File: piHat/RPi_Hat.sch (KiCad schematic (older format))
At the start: 5 parts, among them J1 RPi_GPIO

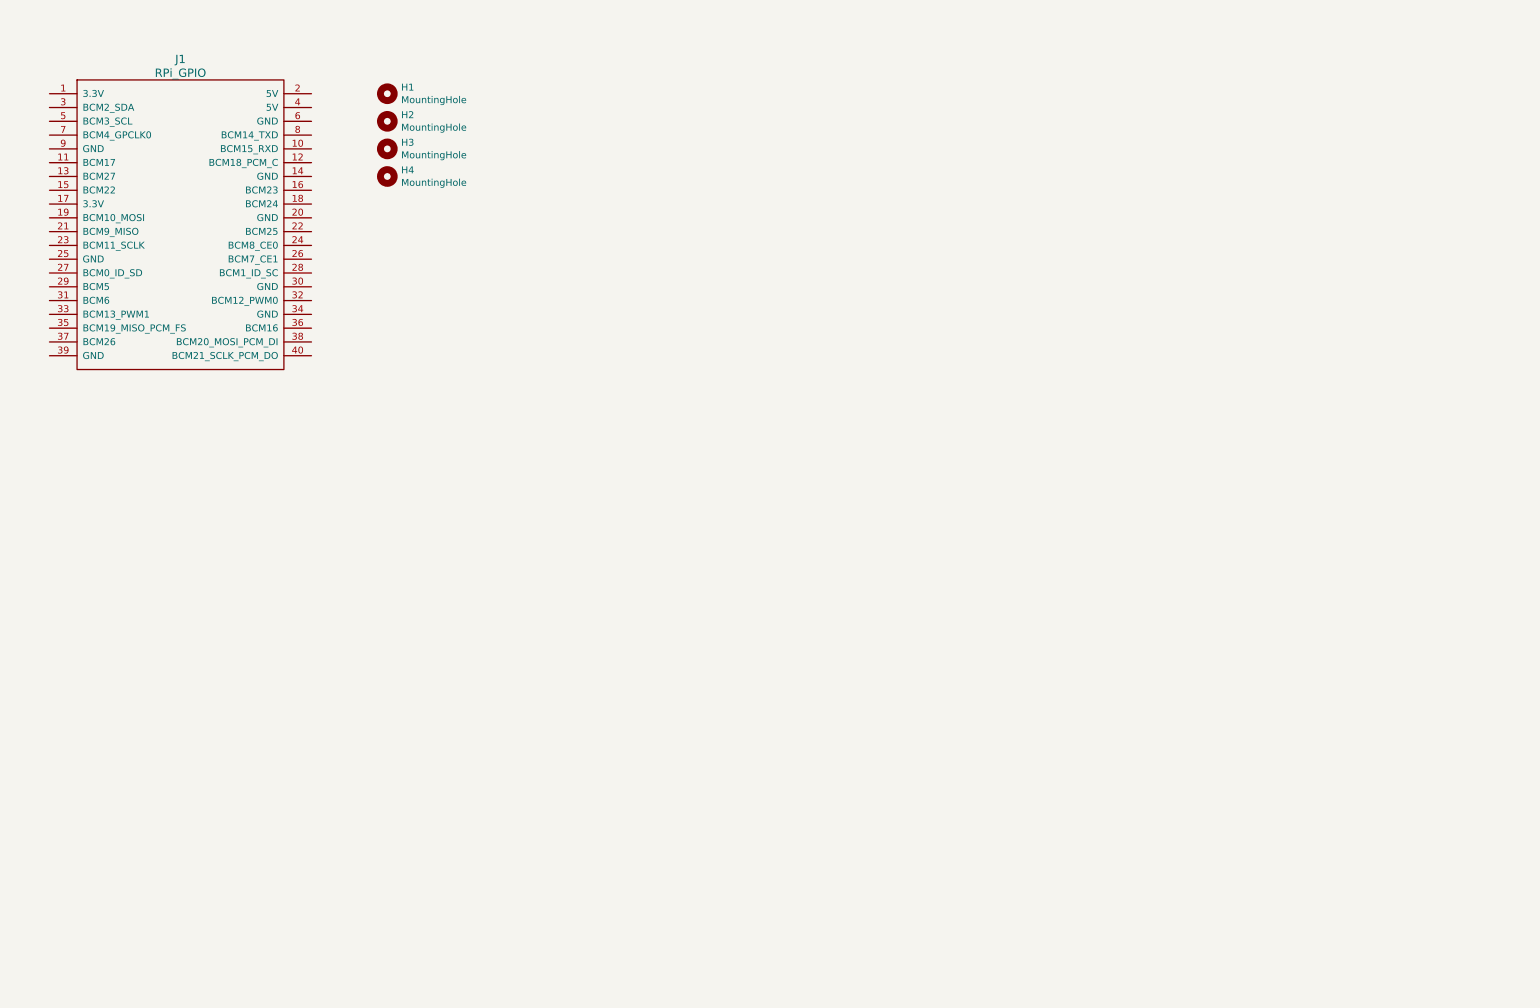
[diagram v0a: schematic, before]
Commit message: add pi HAT schematic (spid hat as template)
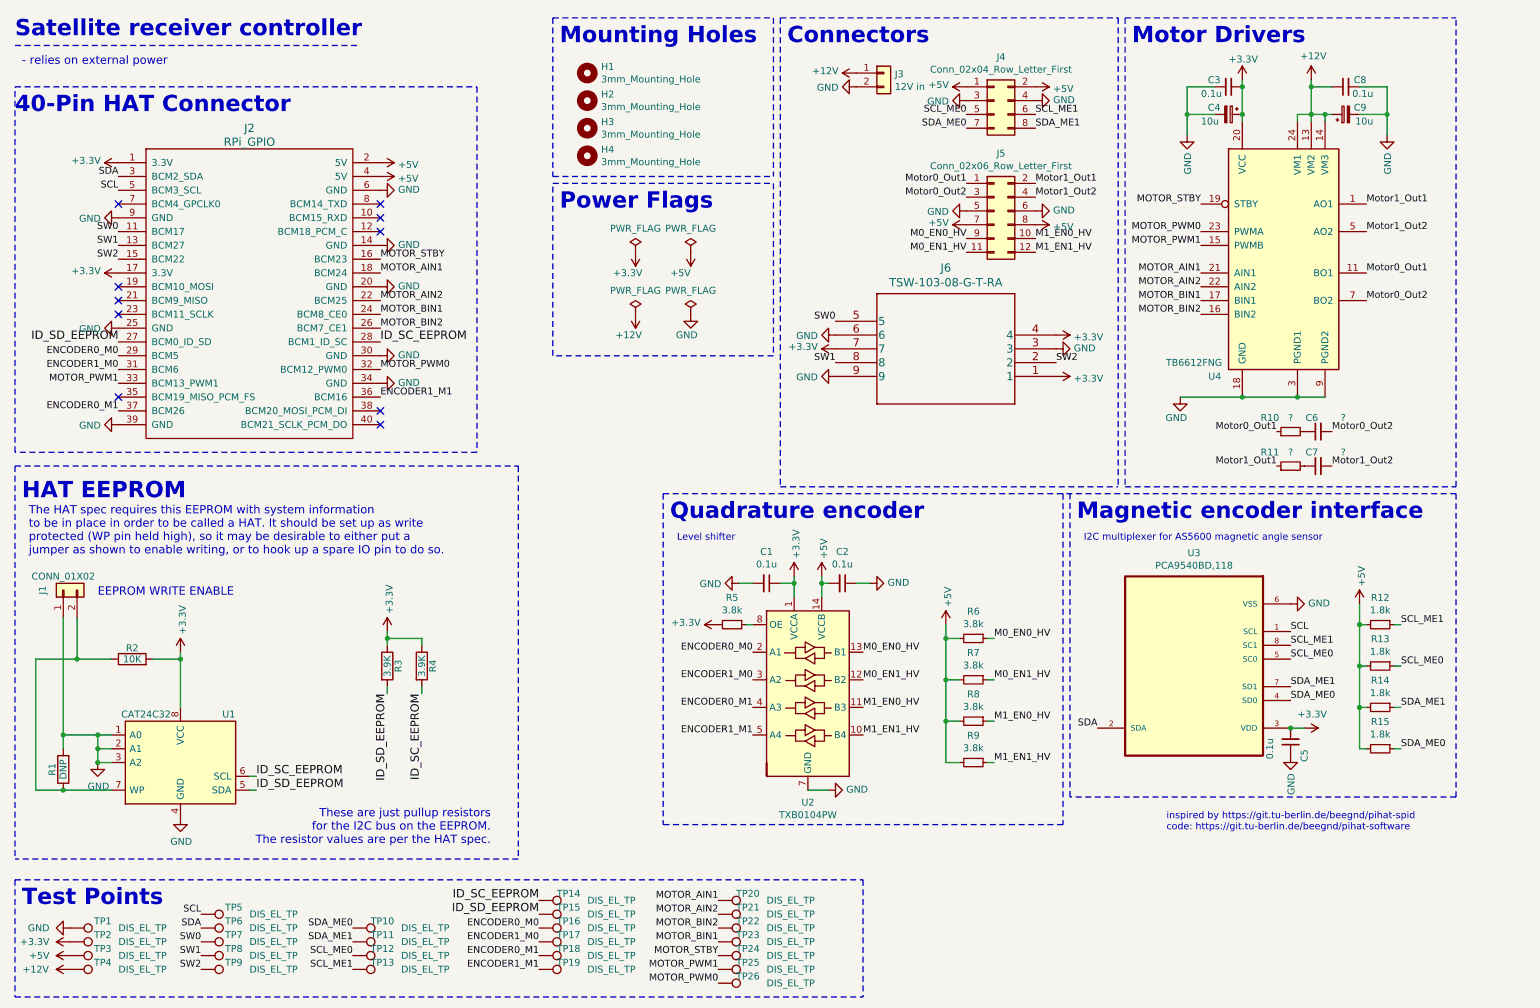
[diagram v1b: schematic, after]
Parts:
- added C1, C2, C3, C5, C8: 0.1u, Capacitor_SMD:C_0805_2012Metric_Pad1.18x1.45mm_HandSolder, symbol Device:C_Small
- added C4, C9: 10u, Capacitor_SMD:C_0805_2012Metric_Pad1.18x1.45mm_HandSolder, symbol Device:CP_Small
- added C6, C7: ?, Capacitor_SMD:C_0805_2012Metric_Pad1.18x1.45mm_HandSolder, symbol Device:C_Small
- added J1: CONN_01X02, Connector_PinHeader_2.54mm:PinHeader_1x02_P2.54mm_Vertical, symbol Connector_Generic:Conn_01x02
- added J3: 12V in, Connector_PinHeader_2.54mm:PinHeader_1x02_P2.54mm_Horizontal, symbol Connector_Generic:Conn_01x02
- added J4: Conn_02x04_Row_Letter_First, Connector_PinHeader_2.54mm:PinHeader_2x04_P2.54mm_Horizontal, symbol Connector_Generic:Conn_02x04_Odd_Even
- added J5: Conn_02x06_Row_Letter_First, Connector_PinHeader_2.54mm:PinHeader_2x06_P2.54mm_Horizontal, symbol Connector_Generic:Conn_02x06_Odd_Even
- added J6: TSW-103-08-G-T-RA, piHat:TSW-103-08-G-T-RA, symbol RPi_Hat:TSW-103-08-G-T-RA
- added R1: DNP, Resistor_SMD:R_0805_2012Metric_Pad1.20x1.40mm_HandSolder, symbol Device:R
- added R10, R11: ?, Resistor_SMD:R_0805_2012Metric_Pad1.20x1.40mm_HandSolder, symbol Device:R_Small
- added R12, R13, R14, R15: 1.8k, Resistor_SMD:R_0805_2012Metric_Pad1.20x1.40mm_HandSolder, symbol Device:R_Small
- added R2: 10K, Resistor_SMD:R_0805_2012Metric_Pad1.20x1.40mm_HandSolder, symbol Device:R
- added R3, R4: 3.9K, Resistor_SMD:R_0805_2012Metric_Pad1.20x1.40mm_HandSolder, symbol Device:R
- added R5, R6, R7, R8, R9: 3.8k, Resistor_SMD:R_0805_2012Metric_Pad1.20x1.40mm_HandSolder, symbol Device:R_Small
- added TP1, TP10, TP11, TP12, TP13, TP14, TP15, TP16, TP17, TP18, TP19, TP2, TP20, TP21, TP22, TP23, TP24, TP25, TP26, TP3, TP4, TP5, TP6, TP7, TP8, TP9: DIS_EL_TP, TestPoint:TestPoint_Pad_D1.0mm, symbol Connector:TestPoint
- added U1: CAT24C32, Package_SO:SOIC-8_3.9x4.9mm_P1.27mm, symbol RPi_Hat:CAT24C32-raspberrypi_hat
- added U2: TXB0104PW, Package_SO:TSSOP-14_4.4x5mm_P0.65mm, symbol Logic_LevelTranslator:TXB0104PW
- added U3: PCA9540BD,118, SOIC127P600X175-8N, symbol RPi_Hat:PCA9540BD,118
- added U4: TB6612FNG, Package_SO:SSOP-24_5.3x8.2mm_P0.65mm, symbol Driver_Motor:TB6612FNG
- H1, H2, H3, H4: value MountingHole -> 3mm_Mounting_Hole; Digikey Part Number (none) -> -; Manufacturer_Part_Number (none) -> -; Mouser Part Number (none) -> -
- J2: renamed from J1; Digikey Part Number (none) -> 1528-1785-ND; Manufacturer_Part_Number (none) -> 2222; Mouser Part Number (none) -> 485-2222
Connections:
- net +3V3: now reaches J2.1 (3.3V)
- net +3V3: now also J2.17 (3.3V), C1.1, C3.1, C4.1, C5.2, J6.1, J6.4, J6.7, R2.2, R3.1, R4.1, R5.2, TP2.1, U1.8 (VCC), U2.1 (VCCA), U3.3 (VDD), U4.20 (VCC)
- net SW0: now reaches J2.11 (BCM17)
- net SW0: now also J6.5, TP7.1
- net SW1: now reaches J2.13 (BCM27)
- net SW1: now also J6.8, TP8.1
- net GND: now reaches J2.14 (GND)
- net GND: now also J2.20 (GND), J2.25 (GND), J2.30 (GND), J2.34 (GND), J2.39 (GND), J2.6 (GND), J2.9 (GND), C1.2, C2.1, C3.2, C4.2, C5.1, C8.2, C9.2, J1.1 (Pin_1), J3.2 (Pin_2), J4.3 (Pin_3), J4.4 (Pin_4), J5.5 (Pin_5), J5.6 (Pin_6), J6.3, J6.6, J6.9, R1.2, TP1.1, U1.1 (A0), U1.2 (A1), U1.3 (A2), U1.4 (GND), U2.7 (GND), U3.6 (VSS), U4.10 (PGND2), U4.18 (GND), U4.3 (PGND1), U4.4 (PGND1), U4.9 (PGND2)
- net SW2: now reaches J2.15 (BCM22)
- net SW2: now also J6.2, TP9.1
- net MOTOR_STBY: now reaches J2.16 (BCM23)
- net MOTOR_STBY: now also TP24.1, U4.19 (STBY)
- net MOTOR_AIN1: now reaches J2.18 (BCM24)
- net MOTOR_AIN1: now also TP20.1, U4.21 (AIN1)
- net +5V: now reaches J2.2 (5V)
- net +5V: now also J2.4 (5V), C2.2, J4.1 (Pin_1), J4.2 (Pin_2), J5.7 (Pin_7), J5.8 (Pin_8), R12.2, R13.2, R14.2, R15.2, R6.2, R7.2, R8.2, R9.2, TP3.1, U2.14 (VCCB)
- net MOTOR_AIN2: now reaches J2.22 (BCM25)
- net MOTOR_AIN2: now also TP21.1, U4.22 (AIN2)
- net MOTOR_BIN1: now reaches J2.24 (BCM8_CE0)
- net MOTOR_BIN1: now also TP23.1, U4.17 (BIN1)
- net MOTOR_BIN2: now reaches J2.26 (BCM7_CE1)
- net MOTOR_BIN2: now also TP22.1, U4.16 (BIN2)
- net ID_SD_EEPROM: now reaches J2.27 (BCM0_ID_SD)
- net ID_SD_EEPROM: now also R3.2, TP15.1, U1.5 (SDA)
- net ID_SC_EEPROM: now reaches J2.28 (BCM1_ID_SC)
- net ID_SC_EEPROM: now also R4.2, TP14.1, U1.6 (SCL)
- net ENCODER0_M0: now reaches J2.29 (BCM5)
- net ENCODER0_M0: now also TP16.1, U2.2 (A1)
- net SDA: now reaches J2.3 (BCM2_SDA)
- net SDA: now also TP6.1, U3.2 (SDA)
- net ENCODER1_M0: now reaches J2.31 (BCM6)
- net ENCODER1_M0: now also TP17.1, U2.3 (A2)
- net MOTOR_PWM0: now reaches J2.32 (BCM12_PWM0)
- net MOTOR_PWM0: now also TP26.1, U4.23 (PWMA)
- net MOTOR_PWM1: now reaches J2.33 (BCM13_PWM1)
- net MOTOR_PWM1: now also TP25.1, U4.15 (PWMB)
- net ENCODER1_M1: now reaches J2.36 (BCM16)
- net ENCODER1_M1: now also TP19.1, U2.5 (A4)
- net ENCODER0_M1: now reaches J2.37 (BCM26)
- net ENCODER0_M1: now also TP18.1, U2.4 (A3)
- net SCL: now reaches J2.5 (BCM3_SCL)
- net SCL: now also TP5.1, U3.1 (SCL)
- new net: R5.1, U2.8 (OE)
- new net: C6.1, R10.2
- new net: C7.1, R11.2
- new net: J1.2 (Pin_2), R1.1, R2.1, U1.7 (WP)
- new net +12V: C8.1, C9.1, J3.1 (Pin_1), TP4.1, U4.13 (VM2), U4.14 (VM3), U4.24 (VM1)
- new net M0_EN0_HV: J5.9 (Pin_9), R6.1, U2.13 (B1)
- new net M0_EN1_HV: J5.11 (Pin_11), R7.1, U2.12 (B2)
- new net M1_EN0_HV: J5.10 (Pin_10), R8.1, U2.11 (B3)
- new net M1_EN1_HV: J5.12 (Pin_12), R9.1, U2.10 (B4)
- new net Motor0_Out1: J5.1 (Pin_1), R10.1, U4.11 (BO1), U4.12 (BO1)
- new net Motor0_Out2: C6.2, J5.3 (Pin_3), U4.7 (BO2), U4.8 (BO2)
- new net Motor1_Out1: J5.2 (Pin_2), R11.1, U4.1 (AO1), U4.2 (AO1)
- new net Motor1_Out2: C7.2, J5.4 (Pin_4), U4.5 (AO2), U4.6 (AO2)
- new net SCL_ME0: J4.5 (Pin_5), R13.1, TP12.1, U3.5 (SC0)
- new net SCL_ME1: J4.6 (Pin_6), R12.1, TP13.1, U3.8 (SC1)
- new net SDA_ME0: J4.7 (Pin_7), R15.1, TP10.1, U3.4 (SD0)
- new net SDA_ME1: J4.8 (Pin_8), R14.1, TP11.1, U3.7 (SD1)
- no-connect marks 0 -> 10
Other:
- note added: "- relies on external power"
- note added: "40-Pin HAT Connector"
- note added: "Connectors"
- note added: "EEPROM WRITE ENABLE"
- note added: "HAT EEPROM"
- note added: "I2C multiplexer for AS5600 magnetic angle sensor"
- note added: "Level shifter"
- note added: "Magnetic encoder interface"
- note added: "Motor Drivers"
- note added: "Mounting Holes"
- note added: "Power Flags\n"
- note added: "Quadrature encoder"
- note added: "Satellite receiver controller"
- note added: "Test Points"
- note added: "The HAT spec requires this EEPROM with system information\nto be in place in order to be called a HAT. It should be set up as write\nprotected (WP pin held high), so it may be desirable to either put a \njumper as shown to enable writing, or to hook up a spare IO pin to do so."
- note added: "These are just pullup resistors \nfor the I2C bus on the EEPROM.\nThe resistor values are per the HAT spec."
- note added: "inspired by https://git.tu-berlin.de/beegnd/pihat-spid\ncode: https://git.tu-berlin.de/beegnd/pihat-software"
- moved on the sheet: H1, H2, H3, H4, J2

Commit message: finalize PCB layout
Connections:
- net Motor1_Out1: now also U4.5 (AO2), U4.6 (AO2); no longer U4.1 (AO1), U4.2 (AO1)
- net Motor1_Out2: now also U4.1 (AO1), U4.2 (AO1); no longer U4.5 (AO2), U4.6 (AO2)
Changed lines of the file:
@@
 Text Label 8050 1900 0    50   ~ 0
 Motor1_Out2
-Text Label 9800 3600 2    50   ~ 0
-Motor0_Out1
-Text Label 10200 3600 0    50   ~ 0
-Motor0_Out2
 $Comp
 L Device:C_Small C6
@@
 	1    0    0    -1
 $EndComp
-Text Label 10200 3850 0    50   ~ 0
-Motor1_Out2
-Text Label 9800 3850 2    50   ~ 0
-Motor1_Out1
 $Comp
 L Device:R_Small R11
@@
 Wire Notes Line
 	6200 4000 8650 4000
+Text Label 10450 1950 0    50   ~ 0
+Motor1_Out2
 Text Label 10450 2150 0    50   ~ 0
-Motor1_Out2
-Text Label 10450 1950 0    50   ~ 0
 Motor1_Out1
 Text Label 10450 2650 0    50   ~ 0
@@
 Text Label 10450 2450 0    50   ~ 0
 Motor0_Out1
+Text Label 10200 3600 0    50   ~ 0
+Motor0_Out2
+Text Label 10200 3850 0    50   ~ 0
+Motor1_Out2
+Text Label 9800 3850 2    50   ~ 0
+Motor1_Out1
+Text Label 9800 3600 2    50   ~ 0
+Motor0_Out1
 $EndSCHEMATC

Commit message: adjust compontens, add BOM
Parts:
- C1, C2, C3, C5, C8: mpn (none) -> 08055C104KAT2A
- C4, C9: Manufacturer_Part_Number CL21A106KOQNNNE -> CL21A106KOQNNNE; mpn (none) -> CL21A106KOQNNNE
- C6, C7, R10, R11: value ? -> DNP; Digikey Part Number ? -> (none); Manufacturer_Part_Number ? -> (none)
- H1, H2, H3, H4, R1, TP1, TP10, TP11, TP12, TP13, TP14, TP15, TP16, TP17, TP18, TP19, TP2, TP20, TP21, TP22, TP23, TP24, TP25, TP26, TP3, TP4, TP5, TP6, TP7, TP8, TP9: Digikey Part Number - -> (none); Manufacturer_Part_Number - -> (none)
- J1: mpn (none) -> 77311-118-02LF
- J2: Digikey Part Number 1528-1785-ND -> S7123-ND; mpn (none) -> PPPC202LFBN-RC
- J3: mpn (none) -> PH1RB-02-UA
- J4: mpn (none) -> PH2RA-08-UA
- J5: mpn (none) -> PH2RA-12-UA
- J6: mpn (none) -> TSW-103-08-G-T-RA
- R12, R13, R14, R15: mpn (none) -> CRGCQ0805F1K8
- R2: mpn (none) -> CRCW080510K0FKEAC
- R3, R4: mpn (none) -> ERA-6AED392V
- R5, R6, R7, R8, R9: mpn (none) -> PAT0805E3791BST1
- U1: mpn (none) -> CAT24C32WI-GT3
- U2: value TXB0104PW -> TXS0104E; Digikey Part Number 296-21929-1-ND -> 296-34699-5-ND; Mouser Part Number 595-TXB0104PWR -> 595-TXS0104ED; mpn (none) -> TXS0104ED
- U3: mpn (none) -> PCA9540BD 118
- U4: mpn (none) -> TB6612FNG C 8 EL
